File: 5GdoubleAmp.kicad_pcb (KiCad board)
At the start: 4 copper layers, 27.8 x 25 mm, 129 parts, among them J1 Conn_Coaxial, J2 Conn_Coaxial, J3 Conn_01x06, U1 SE5004L

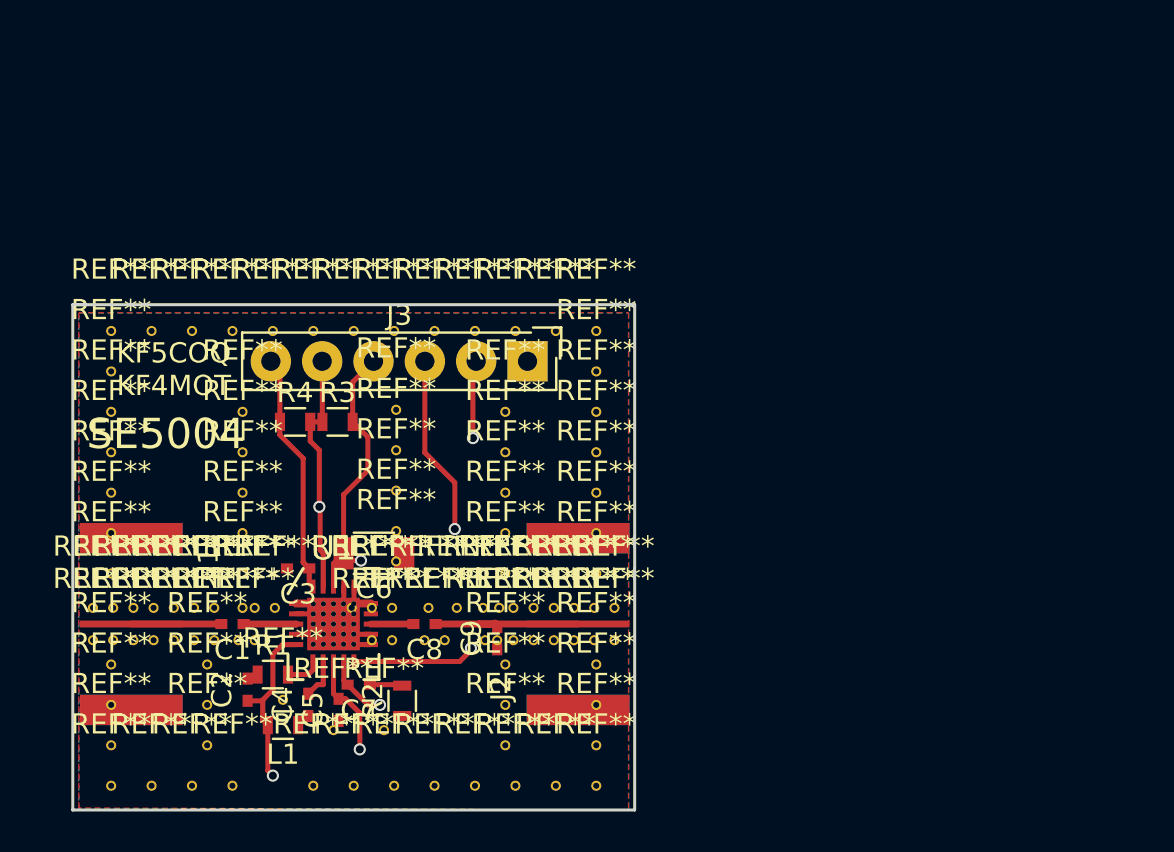
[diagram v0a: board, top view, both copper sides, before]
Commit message: Add files via upload
Added mounting holes, fixes ground via labels, used smaller pins, further decreased overall layout size
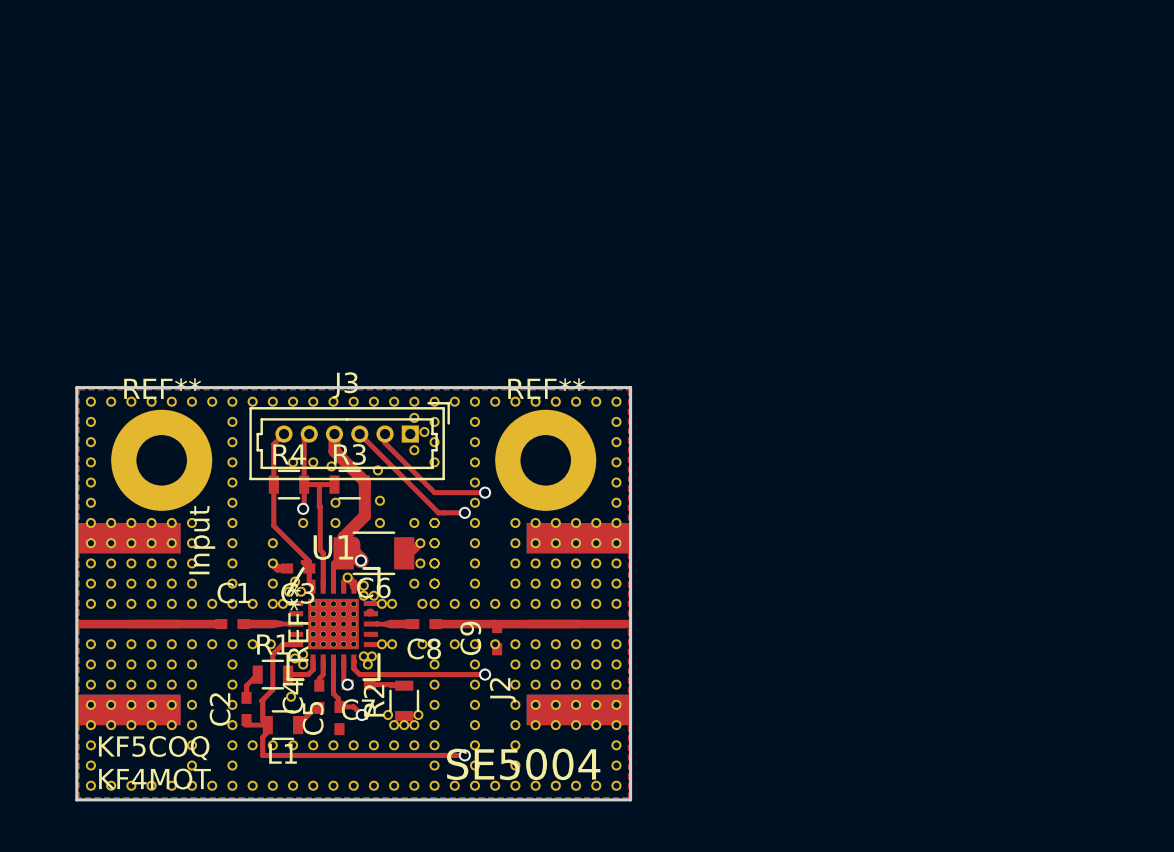
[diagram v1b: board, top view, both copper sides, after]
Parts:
- removed the REF** at (142.2, 111.0)
- removed the REF** at (144.0, 94.5)
- removed the REF** at (139.5, 90.5)
- removed the REF** at (141.5, 90.5)
- removed the REF** at (143.5, 90.5)
- removed the REF** at (145.5, 90.5)
- removed the REF** at (147.5, 90.5)
- removed the REF** at (149.5, 90.5)
- removed the REF** at (151.5, 90.5)
- removed the REF** at (153.5, 90.5)
- removed the REF** at (155.5, 90.5)
- removed the REF** at (157.5, 90.5)
- removed the REF** at (144.0, 96.5)
- removed the REF** at (159.5, 90.5)
- removed the REF** at (161.5, 90.5)
- removed the REF** at (144.0, 98.5)
- removed the REF** at (144.0, 100.5)
- removed the REF** at (144.0, 102.5)
- removed the REF** at (157.0, 94.5)
- removed the REF** at (157.0, 96.5)
- removed the REF** at (157.0, 98.5)
- removed the REF** at (157.0, 100.5)
- removed the REF** at (157.0, 102.5)
- removed the REF** at (142.2, 109.0)
- removed the REF** at (151.6, 94.4)
- removed the REF** at (151.6, 96.4)
- removed the REF** at (151.6, 98.4)
- removed the REF** at (151.6, 100.4)
- removed the REF** at (151.6, 101.9)
- removed the REF** at (149.4, 104.2)
- removed the REF** at (150.4, 104.2)
- removed the REF** at (151.4, 104.2)
- removed the REF** at (153.2, 104.2)
- removed the REF** at (154.6, 104.2)
- removed the REF** at (142.2, 107.0)
- removed the REF** at (155.9, 104.2)
- removed the REF** at (156.7, 104.2)
- removed the REF** at (157.4, 104.2)
- removed the REF** at (158.4, 104.2)
- removed the REF** at (159.4, 104.2)
- removed the REF** at (160.4, 104.2)
- removed the REF** at (161.4, 104.2)
- removed the REF** at (162.4, 104.2)
- removed the REF** at (151.4, 105.8)
- removed the REF** at (151.0, 110.2)
- removed the REF** at (153.0, 105.8)
- removed the REF** at (154.0, 105.8)
- removed the REF** at (156.0, 105.8)
- removed the REF** at (156.6, 105.8)
- removed the REF** at (157.4, 105.8)
- removed the REF** at (158.4, 105.8)
- removed the REF** at (159.4, 105.8)
- removed the REF** at (160.4, 105.8)
- removed the REF** at (161.4, 105.8)
- removed the REF** at (162.4, 105.8)
- removed the REF** at (146.0, 108.8)
- removed the REF** at (145.6, 104.2)
- removed the REF** at (144.6, 104.2)
- removed the REF** at (144.0, 104.2)
- removed the REF** at (142.6, 104.2)
- removed the REF** at (141.6, 104.2)
- removed the REF** at (140.6, 104.2)
- removed the REF** at (139.6, 104.2)
- removed the REF** at (138.6, 104.2)
- removed the REF** at (137.6, 104.2)
- removed the REF** at (148.5, 110.2)
- removed the REF** at (144.6, 105.8)
- removed the REF** at (143.8, 105.8)
- removed the REF** at (142.6, 105.8)
- removed the REF** at (141.6, 105.8)
- removed the REF** at (140.6, 105.8)
- removed the REF** at (139.6, 105.8)
- removed the REF** at (138.6, 105.8)
- removed the REF** at (137.6, 105.8)
- removed the REF** at (157.0, 111.0)
- removed the REF** at (137.5, 111.0)
- removed the REF** at (157.0, 109.0)
- removed the REF** at (161.5, 111.0)
- removed the REF** at (161.5, 102.5)
- removed the REF** at (161.5, 100.5)
- removed the REF** at (161.5, 98.5)
- removed the REF** at (157.0, 107.0)
- removed the REF** at (161.5, 96.5)
- removed the REF** at (161.5, 94.5)
- removed the REF** at (161.5, 92.5)
- removed the REF** at (137.5, 102.5)
- removed the REF** at (137.5, 100.5)
- removed the REF** at (137.5, 98.5)
- removed the REF** at (137.5, 96.5)
- removed the REF** at (137.5, 94.5)
- removed the REF** at (137.5, 92.5)
- removed the REF** at (137.5, 90.5)
- added ?: muwave_arcstub, muwave_arcstub, F.Cu at (150.7, 105.0)
- added ?: 1pin, SKY:.3via, F.Cu at (149.0, 104.5)
- added ?: 1pin, SKY:.3via, F.Cu at (149.5, 104.5)
- added ?: 1pin, SKY:.3via, F.Cu at (147.5, 105.0)
- added ?: 1pin, SKY:.3via, F.Cu at (148.0, 105.0)
- added ?: 1pin, SKY:.3via, F.Cu at (148.5, 105.0)
- added ?: 1pin, SKY:.3via, F.Cu at (149.0, 105.0)
- added ?: 1pin, SKY:.3via, F.Cu at (149.5, 105.0)
- added ?: 1pin, SKY:.3via, F.Cu at (147.5, 105.5)
- added ?: 1pin, SKY:.3via, F.Cu at (148.0, 105.5)
- added ?: 1pin, SKY:.3via, F.Cu at (148.5, 105.5)
- added ?: 1pin, SKY:.3via, F.Cu at (147.5, 104.0)
- added ?: 1pin, SKY:.3via, F.Cu at (149.0, 105.5)
- added ?: 1pin, SKY:.3via, F.Cu at (149.5, 105.5)
- added ?: 1pin, SKY:.3via, F.Cu at (147.5, 106.0)
- added ?: 1pin, SKY:.3via, F.Cu at (148.0, 106.0)
- added ?: 1pin, SKY:.3via, F.Cu at (148.5, 106.0)
- added ?: 1pin, SKY:.3via, F.Cu at (149.0, 106.0)
- added ?: 1pin, SKY:.3via, F.Cu at (148.0, 104.0)
- added ?: 1pin, SKY:.3via, F.Cu at (148.5, 104.0)
- added ?: 1pin, SKY:.3via, F.Cu at (149.0, 104.0)
- added ?: 1pin, SKY:.3via, F.Cu at (149.5, 104.0)
- added ?: 1pin, SKY:.3via, F.Cu at (147.5, 104.5)
- added ?: 1pin, SKY:.3via, F.Cu at (148.0, 104.5)
- added ?: 1pin, SKY:.3via, F.Cu at (148.5, 104.5)
- added REF**: 1pin, SKY:.3via, F.Cu at (152.7, 109.5)
- added REF**: 1pin, SKY:.3via, F.Cu at (147.5, 97.0)
- added REF**: 1pin, SKY:.3via, F.Cu at (155.5, 104.0)
- added REF**: 1pin, SKY:.3via, F.Cu at (156.5, 104.0)
- added REF**: 1pin, SKY:.3via, F.Cu at (154.5, 106.0)
- added REF**: 1pin, SKY:.3via, F.Cu at (155.5, 106.0)
- added REF**: 1pin, SKY:.3via, F.Cu at (156.5, 106.0)
- added REF**: 1pin, SKY:.3via, F.Cu at (157.5, 100.0)
- added REF**: 1pin, SKY:.3via, F.Cu at (157.5, 101.0)
- added REF**: 1pin, SKY:.3via, F.Cu at (157.5, 102.0)
- added REF**: 1pin, SKY:.3via, F.Cu at (157.5, 103.0)
- added REF**: 1pin, SKY:.3via, F.Cu at (141.5, 100.0)
- added REF**: 1pin, SKY:.3via, F.Cu at (150.7, 97.4)
- added REF**: 1pin, SKY:.3via, F.Cu at (141.5, 101.0)
- added REF**: 1pin, SKY:.3via, F.Cu at (141.5, 102.0)
- added REF**: 1pin, SKY:.3via, F.Cu at (141.5, 103.0)
- added REF**: 1pin, SKY:.3via, F.Cu at (157.5, 112.0)
- added REF**: 1pin, SKY:.3via, F.Cu at (157.5, 111.0)
- added REF**: 1pin, SKY:.3via, F.Cu at (157.5, 110.0)
- added REF**: 1pin, SKY:.3via, F.Cu at (157.5, 109.0)
- added REF**: 1pin, SKY:.3via, F.Cu at (157.5, 108.0)
- added REF**: 1pin, SKY:.3via, F.Cu at (157.5, 107.0)
- added REF**: 1pin, SKY:.3via, F.Cu at (150.8, 98.9)
- added REF**: 1pin, SKY:.3via, F.Cu at (141.5, 112.0)
- added REF**: 1pin, SKY:.3via, F.Cu at (141.5, 111.0)
- added REF**: 1pin, SKY:.3via, F.Cu at (141.5, 110.0)
- added REF**: 1pin, SKY:.3via, F.Cu at (141.5, 109.0)
- added REF**: 1pin, SKY:.3via, F.Cu at (141.5, 108.0)
- added REF**: 1pin, SKY:.3via, F.Cu at (141.5, 107.0)
- added REF**: 1pin, SKY:.3via, F.Cu at (151.4, 106.0)
- added REF**: 1pin, SKY:.3via, F.Cu at (152.9, 106.0)
- added REF**: 1pin, SKY:.3via, F.Cu at (153.5, 106.0)
- added REF**: 1pin, SKY:.3via, F.Cu at (157.5, 106.0)
- added REF**: 1pin, SKY:.3via, F.Cu at (148.6, 99.0)
- added REF**: 1pin, SKY:.3via, F.Cu at (151.4, 104.0)
- added REF**: 1pin, SKY:.3via, F.Cu at (152.9, 104.0)
- added REF**: 1pin, SKY:.3via, F.Cu at (153.5, 104.0)
- added REF**: 1pin, SKY:.3via, F.Cu at (157.5, 104.0)
- added REF**: 1pin, SKY:.3via, F.Cu at (145.4, 106.0)
- added REF**: 1pin, SKY:.3via, F.Cu at (144.5, 106.0)
- added REF**: 1pin, SKY:.3via, F.Cu at (143.5, 106.0)
- added REF**: 1pin, SKY:.3via, F.Cu at (142.5, 106.0)
- added REF**: 1pin, SKY:.3via, F.Cu at (141.5, 106.0)
- added REF**: 1pin, SKY:.3via, F.Cu at (145.5, 104.0)
- added REF**: 1pin, SKY:.3via, F.Cu at (148.6, 100.0)
- added REF**: 1pin, SKY:.3via, F.Cu at (144.5, 104.0)
- added REF**: 1pin, SKY:.3via, F.Cu at (143.5, 104.0)
- added REF**: 1pin, SKY:.3via, F.Cu at (142.5, 104.0)
- added REF**: 1pin, SKY:.3via, F.Cu at (141.5, 104.0)
- added REF**: MountingHole_2.5mm_Pad, Mounting_Holes:MountingHole_2.5mm_Pad, F.Cu at (159.0, 96.9)
- added REF**: 1pin, SKY:.3via, F.Cu at (162.5, 111.0)
- added REF**: 1pin, SKY:.3via, F.Cu at (162.5, 112.0)
- added REF**: 1pin, SKY:.3via, F.Cu at (162.5, 113.0)
- added REF**: 1pin, SKY:.3via, F.Cu at (160.5, 113.0)
- added REF**: 1pin, SKY:.3via, F.Cu at (150.8, 100.0)
- added REF**: 1pin, SKY:.3via, F.Cu at (158.5, 113.0)
- added REF**: 1pin, SKY:.3via, F.Cu at (156.5, 113.0)
- added REF**: 1pin, SKY:.3via, F.Cu at (154.5, 113.0)
- added REF**: 1pin, SKY:.3via, F.Cu at (152.5, 113.0)
- added REF**: 1pin, SKY:.3via, F.Cu at (150.5, 113.0)
- added REF**: 1pin, SKY:.3via, F.Cu at (147.0, 100.0)
- added REF**: 1pin, SKY:.3via, F.Cu at (148.5, 113.0)
- added REF**: 1pin, SKY:.3via, F.Cu at (146.5, 113.0)
- added REF**: 1pin, SKY:.3via, F.Cu at (145.5, 113.0)
- added REF**: 1pin, SKY:.3via, F.Cu at (144.5, 113.0)
- added REF**: 1pin, SKY:.3via, F.Cu at (142.5, 113.0)
- added REF**: 1pin, SKY:.3via, F.Cu at (140.5, 113.0)
- added REF**: muwave_arcstub, muwave_arcstub, F.Cu at (146.3, 105.0)
- added REF**: 1pin, SKY:.3via, F.Cu at (138.5, 113.0)
- added REF**: 1pin, SKY:.3via, F.Cu at (136.5, 113.0)
- added REF**: 1pin, SKY:.3via, F.Cu at (136.5, 112.0)
- added REF**: 1pin, SKY:.3via, F.Cu at (136.5, 111.0)
- added REF**: 1pin, SKY:.3via, F.Cu at (136.5, 94.0)
- added REF**: 1pin, SKY:.3via, F.Cu at (136.5, 95.0)
- added REF**: 1pin, SKY:.3via, F.Cu at (136.5, 96.0)
- added REF**: 1pin, SKY:.3via, F.Cu at (136.5, 97.0)
- added REF**: 1pin, SKY:.3via, F.Cu at (136.5, 98.0)
- added REF**: 1pin, SKY:.3via, F.Cu at (136.5, 99.0)
- added REF**: 1pin, SKY:.3via, F.Cu at (149.2, 102.7)
- added REF**: 1pin, SKY:.3via, F.Cu at (137.5, 94.0)
- added REF**: 1pin, SKY:.3via, F.Cu at (138.5, 94.0)
- added REF**: 1pin, SKY:.3via, F.Cu at (139.5, 94.0)
- added REF**: 1pin, SKY:.3via, F.Cu at (140.5, 94.0)
- added REF**: 1pin, SKY:.3via, F.Cu at (141.5, 94.0)
- added REF**: 1pin, SKY:.3via, F.Cu at (142.5, 94.0)
- added REF**: 1pin, SKY:.3via, F.Cu at (143.5, 94.0)
- added REF**: 1pin, SKY:.3via, F.Cu at (144.5, 94.0)
- added REF**: 1pin, SKY:.3via, F.Cu at (145.5, 94.0)
- added REF**: 1pin, SKY:.3via, F.Cu at (146.5, 94.0)
- added REF**: 1pin, SKY:.3via, F.Cu at (146.0, 104.0)
- added REF**: 1pin, SKY:.3via, F.Cu at (147.5, 94.0)
- added REF**: 1pin, SKY:.3via, F.Cu at (148.5, 94.0)
- added REF**: 1pin, SKY:.3via, F.Cu at (149.5, 94.0)
- added REF**: 1pin, SKY:.3via, F.Cu at (150.5, 94.0)
- added REF**: 1pin, SKY:.3via, F.Cu at (151.5, 94.0)
- added REF**: 1pin, SKY:.3via, F.Cu at (152.5, 94.0)
- added REF**: 1pin, SKY:.3via, F.Cu at (153.5, 94.0)
- added REF**: 1pin, SKY:.3via, F.Cu at (154.5, 94.0)
- added REF**: 1pin, SKY:.3via, F.Cu at (155.5, 94.0)
- added REF**: 1pin, SKY:.3via, F.Cu at (156.5, 94.0)
- added REF**: 1pin, SKY:.3via, F.Cu at (151.2, 109.5)
- added REF**: 1pin, SKY:.3via, F.Cu at (150.9, 106.0)
- added REF**: 1pin, SKY:.3via, F.Cu at (157.5, 94.0)
- added REF**: 1pin, SKY:.3via, F.Cu at (158.5, 94.0)
- added REF**: 1pin, SKY:.3via, F.Cu at (159.5, 94.0)
- added REF**: 1pin, SKY:.3via, F.Cu at (160.5, 94.0)
- added REF**: 1pin, SKY:.3via, F.Cu at (161.5, 94.0)
- added REF**: 1pin, SKY:.3via, F.Cu at (162.5, 93.0)
- added REF**: 1pin, SKY:.3via, F.Cu at (162.5, 94.0)
- added REF**: 1pin, SKY:.3via, F.Cu at (162.5, 95.0)
- added REF**: 1pin, SKY:.3via, F.Cu at (162.5, 96.0)
- added REF**: 1pin, SKY:.3via, F.Cu at (162.5, 97.0)
- added REF**: 1pin, SKY:.3via, F.Cu at (150.9, 104.0)
- added REF**: 1pin, SKY:.3via, F.Cu at (162.5, 98.0)
- added REF**: 1pin, SKY:.3via, F.Cu at (162.5, 99.0)
- added REF**: 1pin, SKY:.3via, F.Cu at (158.5, 100.0)
- added REF**: 1pin, SKY:.3via, F.Cu at (159.5, 100.0)
- added REF**: 1pin, SKY:.3via, F.Cu at (160.5, 100.0)
- added REF**: 1pin, SKY:.3via, F.Cu at (161.5, 100.0)
- added REF**: 1pin, SKY:.3via, F.Cu at (162.5, 100.0)
- added REF**: 1pin, SKY:.3via, F.Cu at (158.5, 101.0)
- added REF**: 1pin, SKY:.3via, F.Cu at (159.5, 101.0)
- added REF**: 1pin, SKY:.3via, F.Cu at (160.5, 101.0)
- added REF**: 1pin, SKY:.3via, F.Cu at (150.5, 103.6)
- added REF**: 1pin, SKY:.3via, F.Cu at (161.5, 101.0)
- added REF**: 1pin, SKY:.3via, F.Cu at (162.5, 101.0)
- added REF**: 1pin, SKY:.3via, F.Cu at (158.5, 102.0)
- added REF**: 1pin, SKY:.3via, F.Cu at (159.5, 102.0)
- added REF**: 1pin, SKY:.3via, F.Cu at (160.5, 102.0)
- added REF**: 1pin, SKY:.3via, F.Cu at (161.5, 102.0)
- added REF**: 1pin, SKY:.3via, F.Cu at (162.5, 102.0)
- added REF**: 1pin, SKY:.3via, F.Cu at (158.5, 103.0)
- added REF**: 1pin, SKY:.3via, F.Cu at (159.5, 103.0)
- added REF**: 1pin, SKY:.3via, F.Cu at (160.5, 103.0)
- added REF**: 1pin, SKY:.3via, F.Cu at (150.0, 103.1)
- added REF**: 1pin, SKY:.3via, F.Cu at (161.5, 103.0)
- added REF**: 1pin, SKY:.3via, F.Cu at (162.5, 103.0)
- added REF**: 1pin, SKY:.3via, F.Cu at (158.5, 104.0)
- added REF**: 1pin, SKY:.3via, F.Cu at (159.5, 104.0)
- added REF**: 1pin, SKY:.3via, F.Cu at (160.5, 104.0)
- added REF**: 1pin, SKY:.3via, F.Cu at (161.5, 104.0)
- added REF**: 1pin, SKY:.3via, F.Cu at (162.5, 104.0)
- added REF**: 1pin, SKY:.3via, F.Cu at (158.5, 110.0)
- added REF**: 1pin, SKY:.3via, F.Cu at (159.5, 110.0)
- added REF**: 1pin, SKY:.3via, F.Cu at (160.5, 110.0)
- added REF**: 1pin, SKY:.3via, F.Cu at (150.0, 103.6)
- added REF**: 1pin, SKY:.3via, F.Cu at (161.5, 110.0)
- added REF**: 1pin, SKY:.3via, F.Cu at (162.5, 110.0)
- added REF**: 1pin, SKY:.3via, F.Cu at (158.5, 109.0)
- added REF**: 1pin, SKY:.3via, F.Cu at (159.5, 109.0)
- added REF**: 1pin, SKY:.3via, F.Cu at (160.5, 109.0)
- added REF**: 1pin, SKY:.3via, F.Cu at (162.5, 109.0)
- added REF**: 1pin, SKY:.3via, F.Cu at (158.5, 108.0)
- added REF**: 1pin, SKY:.3via, F.Cu at (159.5, 108.0)
- added REF**: 1pin, SKY:.3via, F.Cu at (160.5, 108.0)
- added REF**: 1pin, SKY:.3via, F.Cu at (150.2, 107.0)
- added REF**: 1pin, SKY:.3via, F.Cu at (161.5, 108.0)
- added REF**: 1pin, SKY:.3via, F.Cu at (162.5, 108.0)
- added REF**: 1pin, SKY:.3via, F.Cu at (158.5, 107.0)
- added REF**: 1pin, SKY:.3via, F.Cu at (159.5, 107.0)
- added REF**: 1pin, SKY:.3via, F.Cu at (160.5, 107.0)
- added REF**: 1pin, SKY:.3via, F.Cu at (162.5, 107.0)
- added REF**: 1pin, SKY:.3via, F.Cu at (158.5, 106.0)
- added REF**: 1pin, SKY:.3via, F.Cu at (159.5, 106.0)
- added REF**: 1pin, SKY:.3via, F.Cu at (160.5, 106.0)
- added REF**: 1pin, SKY:.3via, F.Cu at (150.4, 106.6)
- added REF**: 1pin, SKY:.3via, F.Cu at (161.5, 106.0)
- added REF**: 1pin, SKY:.3via, F.Cu at (162.5, 106.0)
- added REF**: 1pin, SKY:.3via, F.Cu at (140.5, 100.0)
- added REF**: 1pin, SKY:.3via, F.Cu at (139.5, 100.0)
- added REF**: 1pin, SKY:.3via, F.Cu at (138.5, 100.0)
- added REF**: 1pin, SKY:.3via, F.Cu at (137.5, 100.0)
- added REF**: 1pin, SKY:.3via, F.Cu at (136.5, 100.0)
- added REF**: 1pin, SKY:.3via, F.Cu at (140.5, 101.0)
- added REF**: 1pin, SKY:.3via, F.Cu at (139.5, 101.0)
- added REF**: 1pin, SKY:.3via, F.Cu at (138.5, 101.0)
- added REF**: 1pin, SKY:.3via, F.Cu at (150.0, 106.6)
- added REF**: 1pin, SKY:.3via, F.Cu at (137.5, 101.0)
- added REF**: 1pin, SKY:.3via, F.Cu at (136.5, 101.0)
- added REF**: 1pin, SKY:.3via, F.Cu at (140.5, 102.0)
- added REF**: 1pin, SKY:.3via, F.Cu at (139.5, 102.0)
- added REF**: 1pin, SKY:.3via, F.Cu at (138.5, 102.0)
- added REF**: 1pin, SKY:.3via, F.Cu at (137.5, 102.0)
- added REF**: 1pin, SKY:.3via, F.Cu at (136.5, 102.0)
- added REF**: 1pin, SKY:.3via, F.Cu at (140.5, 103.0)
- added REF**: 1pin, SKY:.3via, F.Cu at (139.5, 103.0)
- added REF**: 1pin, SKY:.3via, F.Cu at (138.5, 103.0)
- added REF**: 1pin, SKY:.3via, F.Cu at (146.6, 106.7)
- added REF**: 1pin, SKY:.3via, F.Cu at (137.5, 103.0)
- added REF**: 1pin, SKY:.3via, F.Cu at (136.5, 103.0)
- added REF**: 1pin, SKY:.3via, F.Cu at (140.5, 104.0)
- added REF**: 1pin, SKY:.3via, F.Cu at (139.5, 104.0)
- added REF**: 1pin, SKY:.3via, F.Cu at (138.5, 104.0)
- added REF**: 1pin, SKY:.3via, F.Cu at (137.5, 104.0)
- added REF**: 1pin, SKY:.3via, F.Cu at (140.5, 110.0)
- added REF**: 1pin, SKY:.3via, F.Cu at (139.5, 110.0)
- added REF**: 1pin, SKY:.3via, F.Cu at (138.5, 110.0)
- added REF**: 1pin, SKY:.3via, F.Cu at (137.5, 110.0)
- added REF**: 1pin, SKY:.3via, F.Cu at (147.0, 107.0)
- added REF**: 1pin, SKY:.3via, F.Cu at (136.5, 110.0)
- added REF**: 1pin, SKY:.3via, F.Cu at (140.5, 109.0)
- added REF**: 1pin, SKY:.3via, F.Cu at (139.5, 109.0)
- added REF**: 1pin, SKY:.3via, F.Cu at (138.5, 109.0)
- added REF**: 1pin, SKY:.3via, F.Cu at (136.5, 109.0)
- added REF**: 1pin, SKY:.3via, F.Cu at (140.5, 108.0)
- added REF**: 1pin, SKY:.3via, F.Cu at (139.5, 108.0)
- added REF**: 1pin, SKY:.3via, F.Cu at (138.5, 108.0)
- added REF**: 1pin, SKY:.3via, F.Cu at (137.5, 108.0)
- added REF**: 1pin, SKY:.3via, F.Cu at (152.0, 110.0)
- added REF**: 1pin, SKY:.3via, F.Cu at (147.0, 106.5)
- added REF**: 1pin, SKY:.3via, F.Cu at (136.5, 108.0)
- added REF**: 1pin, SKY:.3via, F.Cu at (140.5, 107.0)
- added REF**: 1pin, SKY:.3via, F.Cu at (139.5, 107.0)
- added REF**: 1pin, SKY:.3via, F.Cu at (138.5, 107.0)
- added REF**: 1pin, SKY:.3via, F.Cu at (136.5, 107.0)
- added REF**: 1pin, SKY:.3via, F.Cu at (140.5, 106.0)
- added REF**: 1pin, SKY:.3via, F.Cu at (139.5, 106.0)
- added REF**: 1pin, SKY:.3via, F.Cu at (138.5, 106.0)
- added REF**: 1pin, SKY:.3via, F.Cu at (137.5, 106.0)
- added REF**: 1pin, SKY:.3via, F.Cu at (146.6, 102.9)
- added REF**: MountingHole_2.5mm_Pad, Mounting_Holes:MountingHole_2.5mm_Pad, F.Cu at (140.0, 96.9)
- added REF**: 1pin, SKY:.3via, F.Cu at (146.3, 103.4)
- added REF**: 1pin, SKY:.3via, F.Cu at (146.9, 103.4)
- added REF**: 1pin, SKY:.3via, F.Cu at (152.8, 102.0)
- added REF**: 1pin, SKY:.3via, F.Cu at (152.8, 101.0)
- added REF**: 1pin, SKY:.3via, F.Cu at (152.5, 100.0)
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- renumbered REF** to ?, J1 to Input
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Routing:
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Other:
- board size 27.8 x 25 mm -> 27.4 x 20.4 mm
- net class Default: clearance 0.2 -> 0.1
- net class Power added: clearance 0.2, trace_width 0.8, via_dia 0.6, via_drill 0.4
- net class RF: clearance 0.2 -> 0.48; trace_width 0.341 -> 0.42
- rule trace_clearance: 0.2 -> 0.1
- rule via_min_size: 0.4 -> 0.3

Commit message: Add files via upload
Finalized V1 design with gerber files, made sure stitched vias were tented, modified solder mask to spec
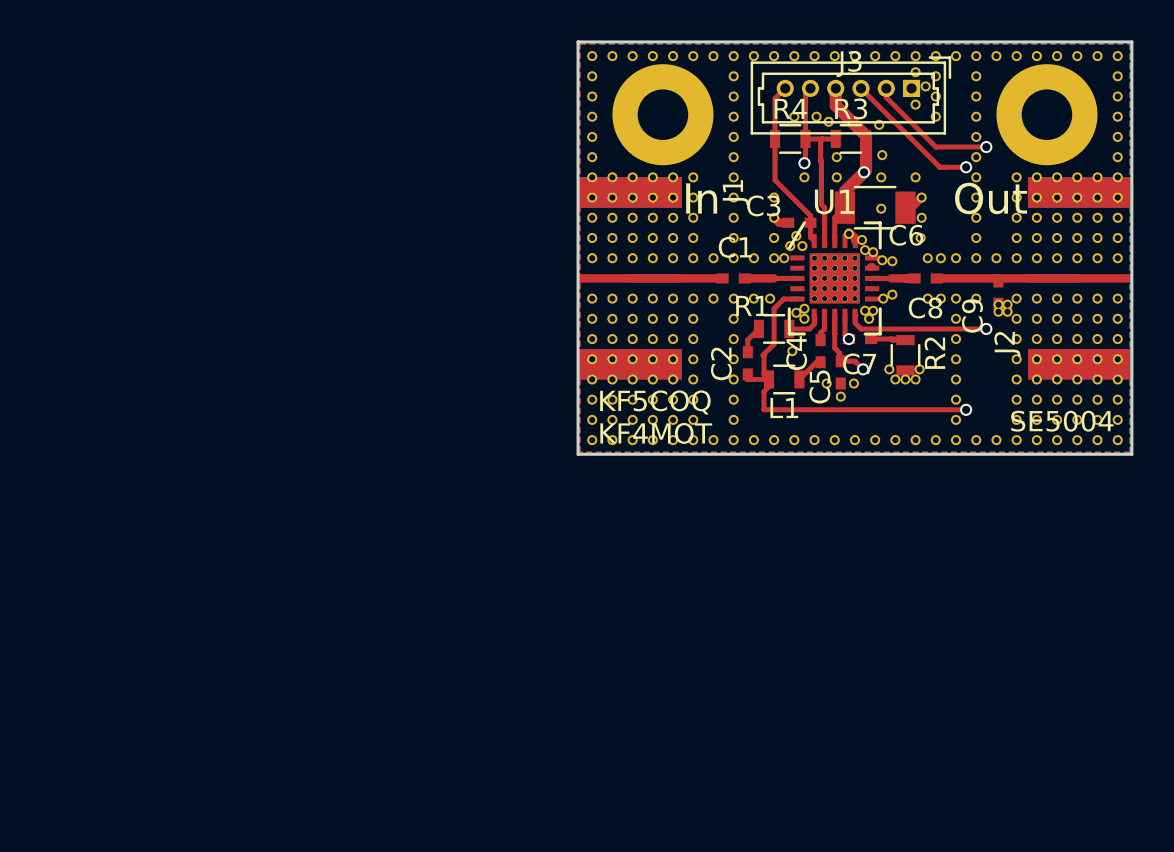
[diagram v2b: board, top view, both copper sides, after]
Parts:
- removed the ? at (150.7, 105.0)
- removed the ? at (149.0, 104.5)
- removed the ? at (149.5, 104.5)
- removed the ? at (147.5, 105.0)
- removed the ? at (148.0, 105.0)
- removed the ? at (148.5, 105.0)
- removed the ? at (149.0, 105.0)
- removed the ? at (149.5, 105.0)
- removed the ? at (147.5, 105.5)
- removed the ? at (148.0, 105.5)
- removed the ? at (148.5, 105.5)
- removed the ? at (149.0, 105.5)
- removed the ? at (149.5, 105.5)
- removed the ? at (147.5, 106.0)
- removed the ? at (148.0, 106.0)
- removed the ? at (148.5, 106.0)
- removed the ? at (149.0, 106.0)
- removed the ? at (149.5, 106.0)
- removed the ? at (148.0, 104.0)
- removed the ? at (148.5, 104.0)
- removed the ? at (149.0, 104.0)
- removed the ? at (149.5, 104.0)
- removed the ? at (147.5, 104.5)
- removed the ? at (148.0, 104.5)
- removed the ? at (148.5, 104.5)
- removed the REF** at (155.5, 104.0)
- removed the REF** at (156.5, 104.0)
- removed the REF** at (155.5, 106.0)
- removed the REF** at (156.5, 106.0)
- removed the REF** at (157.5, 100.0)
- removed the REF** at (157.5, 101.0)
- removed the REF** at (157.5, 102.0)
- removed the REF** at (157.5, 103.0)
- removed the REF** at (141.5, 100.0)
- removed the REF** at (141.5, 101.0)
- removed the REF** at (141.5, 102.0)
- removed the REF** at (141.5, 103.0)
- removed the REF** at (157.5, 112.0)
- removed the REF** at (157.5, 111.0)
- removed the REF** at (157.5, 110.0)
- removed the REF** at (157.5, 109.0)
- removed the REF** at (157.5, 108.0)
- removed the REF** at (157.5, 107.0)
- removed the REF** at (141.5, 113.0)
- removed the REF** at (141.5, 112.0)
- removed the REF** at (141.5, 111.0)
- removed the REF** at (141.5, 110.0)
- removed the REF** at (141.5, 109.0)
- removed the REF** at (141.5, 108.0)
- removed the REF** at (141.5, 107.0)
- removed the REF** at (152.9, 106.0)
- removed the REF** at (157.5, 106.0)
- removed the REF** at (153.5, 104.0)
- removed the REF** at (157.5, 104.0)
- removed the REF** at (141.5, 106.0)
- removed the REF** at (143.5, 104.0)
- removed the REF** at (142.5, 104.0)
- removed the REF** at (141.5, 104.0)
- removed the REF** at (162.5, 111.0)
- removed the REF** at (161.5, 113.0)
- removed the REF** at (160.5, 113.0)
- removed the REF** at (159.5, 113.0)
- removed the REF** at (158.5, 113.0)
- removed the REF** at (157.5, 113.0)
- removed the REF** at (156.5, 113.0)
- removed the REF** at (155.5, 113.0)
- removed the REF** at (154.5, 113.0)
- removed the REF** at (153.5, 113.0)
- removed the REF** at (152.5, 113.0)
- removed the REF** at (151.5, 113.0)
- removed the REF** at (150.5, 113.0)
- removed the REF** at (149.5, 113.0)
- removed the REF** at (148.5, 113.0)
- removed the REF** at (147.5, 113.0)
- removed the REF** at (146.5, 113.0)
- removed the REF** at (145.5, 113.0)
- removed the REF** at (144.5, 113.0)
- removed the REF** at (143.5, 113.0)
- removed the REF** at (142.5, 113.0)
- removed the REF** at (140.5, 113.0)
- removed the REF** at (139.5, 113.0)
- removed the REF** at (146.3, 105.0)
- removed the REF** at (138.5, 113.0)
- removed the REF** at (136.5, 113.0)
- removed the REF** at (136.5, 111.0)
- removed the REF** at (136.5, 94.0)
- removed the REF** at (136.5, 95.0)
- removed the REF** at (136.5, 96.0)
- removed the REF** at (136.5, 97.0)
- removed the REF** at (136.5, 98.0)
- removed the REF** at (136.5, 99.0)
- removed the REF** at (137.5, 94.0)
- removed the REF** at (138.5, 94.0)
- removed the REF** at (139.5, 94.0)
- removed the REF** at (140.5, 94.0)
- removed the REF** at (141.5, 94.0)
- removed the REF** at (142.5, 94.0)
- removed the REF** at (143.5, 94.0)
- removed the REF** at (144.5, 94.0)
- removed the REF** at (145.5, 94.0)
- removed the REF** at (146.5, 94.0)
- removed the REF** at (147.5, 94.0)
- removed the REF** at (148.5, 94.0)
- removed the REF** at (149.5, 94.0)
- removed the REF** at (150.5, 94.0)
- removed the REF** at (151.5, 94.0)
- removed the REF** at (152.5, 94.0)
- removed the REF** at (153.5, 94.0)
- removed the REF** at (154.5, 94.0)
- removed the REF** at (155.5, 94.0)
- removed the REF** at (156.5, 94.0)
- removed the REF** at (157.5, 94.0)
- removed the REF** at (158.5, 94.0)
- removed the REF** at (159.5, 94.0)
- removed the REF** at (160.5, 94.0)
- removed the REF** at (161.5, 94.0)
- removed the REF** at (162.5, 93.0)
- removed the REF** at (162.5, 94.0)
- removed the REF** at (162.5, 95.0)
- removed the REF** at (162.5, 96.0)
- removed the REF** at (162.5, 97.0)
- removed the REF** at (162.5, 98.0)
- removed the REF** at (162.5, 99.0)
- removed the REF** at (158.5, 100.0)
- removed the REF** at (159.5, 100.0)
- removed the REF** at (160.5, 100.0)
- removed the REF** at (161.5, 100.0)
- removed the REF** at (158.5, 101.0)
- removed the REF** at (159.5, 101.0)
- removed the REF** at (160.5, 101.0)
- removed the REF** at (161.5, 101.0)
- removed the REF** at (162.5, 101.0)
- removed the REF** at (158.5, 102.0)
- removed the REF** at (159.5, 102.0)
- removed the REF** at (160.5, 102.0)
- removed the REF** at (161.5, 102.0)
- removed the REF** at (162.5, 102.0)
- removed the REF** at (158.5, 103.0)
- removed the REF** at (159.5, 103.0)
- removed the REF** at (160.5, 103.0)
- removed the REF** at (161.5, 103.0)
- removed the REF** at (162.5, 103.0)
- removed the REF** at (158.5, 104.0)
- removed the REF** at (159.5, 104.0)
- removed the REF** at (160.5, 104.0)
- removed the REF** at (161.5, 104.0)
- removed the REF** at (162.5, 104.0)
- removed the REF** at (158.5, 110.0)
- removed the REF** at (159.5, 110.0)
- removed the REF** at (160.5, 110.0)
- removed the REF** at (161.5, 110.0)
- removed the REF** at (162.5, 110.0)
- removed the REF** at (158.5, 109.0)
- removed the REF** at (159.5, 109.0)
- removed the REF** at (160.5, 109.0)
- removed the REF** at (161.5, 109.0)
- removed the REF** at (162.5, 109.0)
- removed the REF** at (158.5, 108.0)
- removed the REF** at (159.5, 108.0)
- removed the REF** at (160.5, 108.0)
- removed the REF** at (161.5, 108.0)
- removed the REF** at (162.5, 108.0)
- removed the REF** at (158.5, 107.0)
- removed the REF** at (159.5, 107.0)
- removed the REF** at (160.5, 107.0)
- removed the REF** at (161.5, 107.0)
- removed the REF** at (162.5, 107.0)
- removed the REF** at (158.5, 106.0)
- removed the REF** at (159.5, 106.0)
- removed the REF** at (160.5, 106.0)
- removed the REF** at (161.5, 106.0)
- removed the REF** at (162.5, 106.0)
- removed the REF** at (140.5, 100.0)
- removed the REF** at (139.5, 100.0)
- removed the REF** at (138.5, 100.0)
- removed the REF** at (137.5, 100.0)
- removed the REF** at (140.5, 101.0)
- removed the REF** at (139.5, 101.0)
- removed the REF** at (138.5, 101.0)
- removed the REF** at (137.5, 101.0)
- removed the REF** at (136.5, 101.0)
- removed the REF** at (140.5, 102.0)
- removed the REF** at (139.5, 102.0)
- removed the REF** at (138.5, 102.0)
- removed the REF** at (137.5, 102.0)
- removed the REF** at (136.5, 102.0)
- removed the REF** at (140.5, 103.0)
- removed the REF** at (139.5, 103.0)
- removed the REF** at (138.5, 103.0)
- removed the REF** at (137.5, 103.0)
- removed the REF** at (136.5, 103.0)
- removed the REF** at (140.5, 104.0)
- removed the REF** at (139.5, 104.0)
- removed the REF** at (138.5, 104.0)
- removed the REF** at (137.5, 104.0)
- removed the REF** at (140.5, 110.0)
- removed the REF** at (139.5, 110.0)
- removed the REF** at (138.5, 110.0)
- removed the REF** at (137.5, 110.0)
- removed the REF** at (136.5, 110.0)
- removed the REF** at (140.5, 109.0)
- removed the REF** at (139.5, 109.0)
- removed the REF** at (138.5, 109.0)
- removed the REF** at (137.5, 109.0)
- removed the REF** at (136.5, 109.0)
- removed the REF** at (140.5, 108.0)
- removed the REF** at (139.5, 108.0)
- removed the REF** at (138.5, 108.0)
- removed the REF** at (137.5, 108.0)
- removed the REF** at (136.5, 108.0)
- removed the REF** at (140.5, 107.0)
- removed the REF** at (139.5, 107.0)
- removed the REF** at (138.5, 107.0)
- removed the REF** at (137.5, 107.0)
- removed the REF** at (136.5, 107.0)
- removed the REF** at (140.5, 106.0)
- removed the REF** at (139.5, 106.0)
- removed the REF** at (138.5, 106.0)
- removed the REF** at (137.5, 106.0)
- removed the REF** at (137.5, 113.0)
- removed the REF** at (136.5, 104.0)
- removed the REF** at (136.5, 106.0)
- removed the REF** at (153.5, 103.0) (x2)
- removed the REF** at (153.5, 102.0) (x2)
- removed the REF** at (153.5, 101.0) (x2)
- removed the REF** at (153.5, 100.0) (x2)
- removed the REF** at (152.5, 111.0)
- removed the REF** at (151.5, 111.0)
- removed the REF** at (150.5, 111.0)
- removed the REF** at (149.5, 111.0)
- removed the REF** at (148.5, 111.0)
- removed the REF** at (147.5, 111.0)
- removed the REF** at (146.5, 111.0)
- removed the REF** at (145.5, 111.0)
- removed the REF** at (144.5, 111.0)
- removed the REF** at (143.5, 112.0)
- removed the REF** at (143.5, 111.0)
- removed the REF** at (143.5, 110.0)
- removed the REF** at (143.5, 109.0)
- removed the REF** at (143.5, 108.0)
- removed the REF** at (143.5, 107.0)
- removed the REF** at (153.5, 112.0)
- removed the REF** at (153.5, 111.0)
- removed the REF** at (153.5, 110.0)
- removed the REF** at (153.5, 109.0)
- removed the REF** at (153.5, 108.0)
- removed the REF** at (153.5, 107.0)
- removed the REF** at (155.5, 112.0)
- removed the REF** at (155.5, 111.0)
- removed the REF** at (155.5, 110.0)
- removed the REF** at (155.5, 109.0)
- removed the REF** at (155.5, 108.0)
- removed the REF** at (155.5, 107.0)
- removed the REF** at (155.5, 95.0)
- removed the REF** at (155.5, 96.0)
- removed the REF** at (155.5, 97.0)
- removed the REF** at (155.5, 98.0)
- removed the REF** at (155.5, 99.0)
- removed the REF** at (155.5, 100.0)
- removed the REF** at (155.5, 101.0)
- removed the REF** at (155.5, 102.0)
- removed the REF** at (155.5, 103.0)
- removed the REF** at (143.5, 95.0)
- removed the REF** at (143.5, 96.0)
- removed the REF** at (143.5, 97.0)
- removed the REF** at (143.5, 98.0)
- removed the REF** at (143.5, 99.0)
- removed the REF** at (143.5, 100.0)
- removed the REF** at (143.5, 101.0)
- removed the REF** at (143.5, 102.0)
- removed the REF** at (143.5, 103.0)
- added ?: 1pin, SKY:.3via, F.Cu at (172.8, 88.4)
- added ?: 1pin, SKY:.3via, F.Cu at (172.3, 88.4)
- added ?: 1pin, SKY:.3via, F.Cu at (174.3, 87.9)
- added ?: 1pin, SKY:.3via, F.Cu at (173.8, 87.9)
- added ?: 1pin, SKY:.3via, F.Cu at (173.3, 87.9)
- added ?: 1pin, SKY:.3via, F.Cu at (172.8, 87.9)
- added ?: 1pin, SKY:.3via, F.Cu at (172.3, 87.9)
- added ?: 1pin, SKY:.3via, F.Cu at (174.3, 87.4)
- added ?: 1pin, SKY:.3via, F.Cu at (173.8, 87.4)
- added ?: 1pin, SKY:.3via, F.Cu at (173.3, 87.4)
- added ?: 1pin, SKY:.3via, F.Cu at (174.3, 88.9)
- added ?: 1pin, SKY:.3via, F.Cu at (172.8, 87.4)
- added ?: 1pin, SKY:.3via, F.Cu at (172.3, 87.4)
- added ?: 1pin, SKY:.3via, F.Cu at (174.3, 86.9)
- added ?: 1pin, SKY:.3via, F.Cu at (173.8, 86.9)
- added ?: 1pin, SKY:.3via, F.Cu at (173.3, 86.9)
- added ?: 1pin, SKY:.3via, F.Cu at (172.8, 86.9)
- added ?: 1pin, SKY:.3via, F.Cu at (173.8, 88.9)
- added ?: 1pin, SKY:.3via, F.Cu at (173.3, 88.9)
- added ?: 1pin, SKY:.3via, F.Cu at (172.8, 88.9)
- added ?: 1pin, SKY:.3via, F.Cu at (172.3, 88.9)
- added ?: 1pin, SKY:.3via, F.Cu at (174.3, 88.4)
- added ?: 1pin, SKY:.3via, F.Cu at (173.8, 88.4)
- added ?: 1pin, SKY:.3via, F.Cu at (173.3, 88.4)
- added REF**: 1pin, SKY:.3via, F.Cu at (178.6, 86.9)
- added REF**: 1pin, SKY:.3via, F.Cu at (168.3, 94.9)
- added REF**: 1pin, SKY:.3via, F.Cu at (185.3, 84.9)
- added REF**: 1pin, SKY:.3via, F.Cu at (186.3, 84.9)
- added REF**: 1pin, SKY:.3via, F.Cu at (187.3, 84.9)
- added REF**: 1pin, SKY:.3via, F.Cu at (182.3, 83.9)
- added REF**: 1pin, SKY:.3via, F.Cu at (183.3, 83.9)
- added REF**: 1pin, SKY:.3via, F.Cu at (184.3, 83.9)
- added REF**: 1pin, SKY:.3via, F.Cu at (185.3, 83.9)
- added REF**: 1pin, SKY:.3via, F.Cu at (186.3, 83.9)
- added REF**: 1pin, SKY:.3via, F.Cu at (187.3, 83.9)
- added REF**: 1pin, SKY:.3via, F.Cu at (182.3, 82.9)
- added REF**: 1pin, SKY:.3via, F.Cu at (168.3, 93.9)
- added REF**: 1pin, SKY:.3via, F.Cu at (183.3, 82.9)
- added REF**: 1pin, SKY:.3via, F.Cu at (184.3, 82.9)
- added REF**: 1pin, SKY:.3via, F.Cu at (185.3, 82.9)
- added REF**: 1pin, SKY:.3via, F.Cu at (186.3, 82.9)
- added REF**: 1pin, SKY:.3via, F.Cu at (166.3, 86.9)
- added REF**: 1pin, SKY:.3via, F.Cu at (165.3, 86.9)
- added REF**: 1pin, SKY:.3via, F.Cu at (164.3, 86.9)
- added REF**: 1pin, SKY:.3via, F.Cu at (163.3, 86.9)
- added REF**: 1pin, SKY:.3via, F.Cu at (168.3, 92.9)
- added REF**: 1pin, SKY:.3via, F.Cu at (162.3, 86.9)
- added REF**: 1pin, SKY:.3via, F.Cu at (161.3, 86.9)
- added REF**: 1pin, SKY:.3via, F.Cu at (166.3, 85.9)
- added REF**: 1pin, SKY:.3via, F.Cu at (165.3, 85.9)
- added REF**: 1pin, SKY:.3via, F.Cu at (164.3, 85.9)
- added REF**: 1pin, SKY:.3via, F.Cu at (163.3, 85.9)
- added REF**: 1pin, SKY:.3via, F.Cu at (162.3, 85.9)
- added REF**: 1pin, SKY:.3via, F.Cu at (161.3, 85.9)
- added REF**: 1pin, SKY:.3via, F.Cu at (166.3, 84.9)
- added REF**: 1pin, SKY:.3via, F.Cu at (165.3, 84.9)
- added REF**: 1pin, SKY:.3via, F.Cu at (168.3, 91.9)
- added REF**: 1pin, SKY:.3via, F.Cu at (164.3, 84.9)
- added REF**: 1pin, SKY:.3via, F.Cu at (163.3, 84.9)
- added REF**: 1pin, SKY:.3via, F.Cu at (162.3, 84.9)
- added REF**: 1pin, SKY:.3via, F.Cu at (161.3, 84.9)
- added REF**: 1pin, SKY:.3via, F.Cu at (166.3, 83.9)
- added REF**: 1pin, SKY:.3via, F.Cu at (165.3, 83.9)
- added REF**: 1pin, SKY:.3via, F.Cu at (164.3, 83.9)
- added REF**: 1pin, SKY:.3via, F.Cu at (163.3, 83.9)
- added REF**: 1pin, SKY:.3via, F.Cu at (162.3, 83.9)
- added REF**: 1pin, SKY:.3via, F.Cu at (161.3, 83.9)
- added REF**: 1pin, SKY:.3via, F.Cu at (168.3, 90.9)
- added REF**: 1pin, SKY:.3via, F.Cu at (166.3, 82.9)
- added REF**: 1pin, SKY:.3via, F.Cu at (165.3, 82.9)
- added REF**: 1pin, SKY:.3via, F.Cu at (164.3, 82.9)
- added REF**: 1pin, SKY:.3via, F.Cu at (163.3, 82.9)
- added REF**: 1pin, SKY:.3via, F.Cu at (162.3, 82.9)
- added REF**: 1pin, SKY:.3via, F.Cu at (182.3, 88.9)
- added REF**: 1pin, SKY:.3via, F.Cu at (183.3, 88.9)
- added REF**: 1pin, SKY:.3via, F.Cu at (184.3, 88.9)
- added REF**: 1pin, SKY:.3via, F.Cu at (185.3, 88.9)
- added REF**: 1pin, SKY:.3via, F.Cu at (186.3, 88.9)
- added REF**: 1pin, SKY:.3via, F.Cu at (168.3, 89.9)
- added REF**: 1pin, SKY:.3via, F.Cu at (187.3, 88.9)
- added REF**: 1pin, SKY:.3via, F.Cu at (182.3, 89.9)
- added REF**: 1pin, SKY:.3via, F.Cu at (183.3, 89.9)
- added REF**: 1pin, SKY:.3via, F.Cu at (184.3, 89.9)
- added REF**: 1pin, SKY:.3via, F.Cu at (185.3, 89.9)
- added REF**: 1pin, SKY:.3via, F.Cu at (186.3, 89.9)
- added REF**: 1pin, SKY:.3via, F.Cu at (187.3, 89.9)
- added REF**: 1pin, SKY:.3via, F.Cu at (182.3, 90.9)
- added REF**: 1pin, SKY:.3via, F.Cu at (183.3, 90.9)
- added REF**: 1pin, SKY:.3via, F.Cu at (184.3, 90.9)
- added REF**: 1pin, SKY:.3via, F.Cu at (172.9, 93.1)
- added REF**: 1pin, SKY:.3via, F.Cu at (185.3, 90.9)
- added REF**: 1pin, SKY:.3via, F.Cu at (186.3, 90.9)
- added REF**: 1pin, SKY:.3via, F.Cu at (187.3, 90.9)
- added REF**: 1pin, SKY:.3via, F.Cu at (182.3, 91.9)
- added REF**: 1pin, SKY:.3via, F.Cu at (183.3, 91.9)
- added REF**: 1pin, SKY:.3via, F.Cu at (184.3, 91.9)
- added REF**: 1pin, SKY:.3via, F.Cu at (185.3, 91.9)
- added REF**: 1pin, SKY:.3via, F.Cu at (186.3, 91.9)
- added REF**: 1pin, SKY:.3via, F.Cu at (187.3, 91.9)
- added REF**: 1pin, SKY:.3via, F.Cu at (182.3, 92.9)
- added REF**: 1pin, SKY:.3via, F.Cu at (174.2, 93.1)
- added REF**: 1pin, SKY:.3via, F.Cu at (183.3, 92.9)
- added REF**: 1pin, SKY:.3via, F.Cu at (184.3, 92.9)
- added REF**: 1pin, SKY:.3via, F.Cu at (185.3, 92.9)
- added REF**: 1pin, SKY:.3via, F.Cu at (186.3, 92.9)
- added REF**: 1pin, SKY:.3via, F.Cu at (187.3, 92.9)
- added REF**: 1pin, SKY:.3via, F.Cu at (182.3, 93.9)
- added REF**: 1pin, SKY:.3via, F.Cu at (183.3, 93.9)
- added REF**: 1pin, SKY:.3via, F.Cu at (184.3, 93.9)
- added REF**: 1pin, SKY:.3via, F.Cu at (185.3, 93.9)
- added REF**: 1pin, SKY:.3via, F.Cu at (186.3, 93.9)
- added REF**: 1pin, SKY:.3via, F.Cu at (173.6, 93.8)
- added REF**: 1pin, SKY:.3via, F.Cu at (187.3, 93.9)
- added REF**: 1pin, SKY:.3via, F.Cu at (182.3, 94.9)
- added REF**: 1pin, SKY:.3via, F.Cu at (183.3, 94.9)
- added REF**: 1pin, SKY:.3via, F.Cu at (184.3, 94.9)
- added REF**: 1pin, SKY:.3via, F.Cu at (185.3, 94.9)
- added REF**: 1pin, SKY:.3via, F.Cu at (186.3, 94.9)
- added REF**: 1pin, SKY:.3via, F.Cu at (166.3, 88.9)
- added REF**: 1pin, SKY:.3via, F.Cu at (165.3, 88.9)
- added REF**: 1pin, SKY:.3via, F.Cu at (164.3, 88.9)
- added REF**: 1pin, SKY:.3via, F.Cu at (181.8, 89.2)
- added REF**: 1pin, SKY:.3via, F.Cu at (163.3, 88.9)
- added REF**: 1pin, SKY:.3via, F.Cu at (162.3, 88.9)
- added REF**: 1pin, SKY:.3via, F.Cu at (161.3, 88.9)
- added REF**: 1pin, SKY:.3via, F.Cu at (166.3, 89.9)
- added REF**: 1pin, SKY:.3via, F.Cu at (165.3, 89.9)
- added REF**: 1pin, SKY:.3via, F.Cu at (164.3, 89.9)
- added REF**: 1pin, SKY:.3via, F.Cu at (163.3, 89.9)
- added REF**: 1pin, SKY:.3via, F.Cu at (162.3, 89.9)
- added REF**: 1pin, SKY:.3via, F.Cu at (161.3, 89.9)
- added REF**: 1pin, SKY:.3via, F.Cu at (166.3, 90.9)
- added REF**: 1pin, SKY:.3via, F.Cu at (178.6, 88.9)
- added REF**: 1pin, SKY:.3via, F.Cu at (181.8, 89.5)
- added REF**: 1pin, SKY:.3via, F.Cu at (165.3, 90.9)
- added REF**: 1pin, SKY:.3via, F.Cu at (164.3, 90.9)
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- renumbered Input to J1
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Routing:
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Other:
- net class RF: trace_width 0.42 -> 0.25
- rule via_min_size: 0.3 -> 0.254
- board text added: "4"
- board text added: "In"
- board text added: "Out"
